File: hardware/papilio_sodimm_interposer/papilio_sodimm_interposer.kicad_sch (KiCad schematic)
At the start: 1 part, among them U1 Papilio Pro

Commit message: Got it going
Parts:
- removed U1: Papilio Pro, papilo_pro:COCOON_48BIT, symbol Papilio_Pro:Papilio_Pro
- added J1: Papilio Pro, Papilio_Pro:PAPILIO_PRO, symbol Papilio_pro:Papilio_Pro
- added SLOT1: DDR3_204P_SMD, Papilio_Pro:SODIMM_DDR3_EDGE, symbol Things:DDR3_204P_SMD
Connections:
- net +5V: now also J1.VIW1@1 (5V), J1.VIW1@2 (5V), J1.VIW1@3 (5V), J1.VIW1@4 (5V), J1.VIW2@1 (5V), J1.VIW2@2 (5V), SLOT1.4, SLOT1.5, SLOT1.6, SLOT1.7
- net GND: now also J1.GNDW1@1 (GND), J1.GNDW1@2 (GND), J1.GNDW1@3 (GND), J1.GNDW1@4 (GND), J1.GNDW2@1 (GND), J1.GNDW2@2 (GND), SLOT1.127, SLOT1.128, SLOT1.13, SLOT1.133, SLOT1.134, SLOT1.138, SLOT1.139, SLOT1.14, SLOT1.144, SLOT1.145, SLOT1.150, SLOT1.151, SLOT1.155, SLOT1.156, SLOT1.161, SLOT1.162, SLOT1.167, SLOT1.168, SLOT1.172, SLOT1.173, SLOT1.178, SLOT1.179, SLOT1.184, SLOT1.185, SLOT1.189, SLOT1.19, SLOT1.190, SLOT1.195, SLOT1.196, SLOT1.2, SLOT1.20, SLOT1.25, SLOT1.26, SLOT1.3, SLOT1.31, SLOT1.32, SLOT1.37, SLOT1.38, SLOT1.43, SLOT1.48, SLOT1.49, SLOT1.54, SLOT1.55, SLOT1.60, SLOT1.61, SLOT1.66, SLOT1.71, SLOT1.72, SLOT1.8, SLOT1.9, SLOT1.MP
- new net: J1.3V3W1@1 (3.3V), J1.3V3W1@2 (3.3V), J1.3V3W1@3 (3.3V), J1.3V3W1@4 (3.3V), J1.3V3W2@1 (3.3V), J1.3V3W2@2 (3.3V)
- new net +3.3V: SLOT1.22, SLOT1.24
- new net A13_IOR32A_READY: SLOT1.98
- new net B10_IOR31B_~{RECFG}: SLOT1.96
- new net C10_IOR39A: SLOT1.135
- new net C13_IOR32B_DONE: SLOT1.136
- new net C7_IOL40B_1V5: SLOT1.157
- new net CLK16: SLOT1.148
- new net CLK_16: J1.A13
- new net D7_IOL53B_1V5: SLOT1.159
- new net E8_IOL45B_1V5: SLOT1.160
- new net E9_IOL38B_1V5: SLOT1.158
- new net FPGA_CS#: J1.B9, SLOT1.198
- new net FPGA_MISO: J1.B10, SLOT1.192
- new net FPGA_MOSI: J1.B11, SLOT1.194
- new net FPGA_SCLK: J1.B12, SLOT1.200
- new net F_VCCO0&1: SLOT1.164, SLOT1.166
- new net F_VCCO7: SLOT1.170, SLOT1.174
- new net JTAG_TCK: SLOT1.149
- new net JTAG_TDI: SLOT1.153
- new net JTAG_TDO: SLOT1.147
- new net JTAG_TMS: SLOT1.143
- new net LVDS_IOR40_N: SLOT1.193
- new net LVDS_IOR40_P: SLOT1.191
- new net LVDS_IOT32_N: SLOT1.152
- new net LVDS_IOT32_P: SLOT1.154
- new net LVDS_TX1_N: SLOT1.142
- new net LVDS_TX1_P: SLOT1.140
- new net M11_IOR27B_FPGA_TXO: SLOT1.11
- new net R09_I1: SLOT1.63
- new net R09_Q1: SLOT1.65
- new net R10_I1: J1.A10, SLOT1.62
- new net R10_Q1: SLOT1.64
- new net R11_I1: J1.A9, SLOT1.67
- new net R11_Q1: SLOT1.69
- new net R12_I1: J1.A11, SLOT1.68
- new net R12_Q1: SLOT1.70
- new net R13_I1: J1.A1, SLOT1.73
- new net R13_Q1: SLOT1.75
- new net R14_I1: J1.A0, SLOT1.74
- new net R14_Q1: SLOT1.76
- new net R15_I1: J1.A2, SLOT1.77
- new net R15_Q1: SLOT1.79
- new net R16_I1: J1.A5, SLOT1.78
- new net R16_Q1: SLOT1.80
- new net R17_I1: J1.A6, SLOT1.83
- new net R17_Q1: SLOT1.85
- new net R18_I1: J1.A4, SLOT1.84
- new net R18_Q1: SLOT1.86
- new net R19_I1: J1.C1, SLOT1.89
- new net R19_Q1: SLOT1.91
- new net R20_I1: J1.C0, SLOT1.90
- new net R20_Q1: SLOT1.92
- new net R21_I1: J1.C2, SLOT1.95
- new net R21_Q1: SLOT1.97
- new net R22_I1: J1.C5, SLOT1.101
- new net R22_Q1: SLOT1.103
- new net R23_I1: J1.C6, SLOT1.107
- new net R23_Q1: SLOT1.109
- new net R24_I1: J1.C4, SLOT1.113
- new net R24_Q1: SLOT1.115
- new net R25_I1: SLOT1.119
- new net R25_Q1: SLOT1.121
- new net R26_I1: SLOT1.123
- new net R26_Q1: SLOT1.125
- new net R27_I1: SLOT1.129
- new net R27_Q1: SLOT1.131
- new net R28_I1: SLOT1.130
- new net R28_Q1: SLOT1.132
- new net R29_I1: SLOT1.175
- new net R29_Q1: SLOT1.177
- new net R30_I1: SLOT1.180
- new net R30_Q1: SLOT1.176
- new net R31_I1: SLOT1.181
- new net R31_Q1: SLOT1.183
- new net R32_I1: SLOT1.186
- new net R32_Q1: SLOT1.182
- new net R9_I1: J1.A12
- new net RADIO_RECONFIG: SLOT1.146
- new net RX01_I0: SLOT1.27
- new net RX01_I1: J1.C13, SLOT1.29
- new net RX01_Q0: SLOT1.28
- new net RX01_Q1: SLOT1.30
- new net RX02_I0: SLOT1.33
- new net RX02_I1: J1.C14, SLOT1.35
- new net RX02_Q0: SLOT1.34
- new net RX02_Q1: SLOT1.36
- new net RX03_I0: SLOT1.39
- new net RX03_I1: J1.C12, SLOT1.41
- new net RX03_Q0: SLOT1.40
- new net RX03_Q1: SLOT1.42
- new net RX04_I0: SLOT1.45
- new net RX04_I1: J1.C10, SLOT1.47
- new net RX04_Q0: SLOT1.44
- new net RX04_Q1: SLOT1.46
- new net RX05_I1: J1.C9, SLOT1.51
- new net RX05_Q1: SLOT1.53
- new net RX06_I1: J1.C11, SLOT1.50
- new net RX06_Q1: SLOT1.52
- new net RX07_I1: J1.A14, SLOT1.57
- new net RX07_Q1: SLOT1.59
- new net RX08_I1: J1.A15, SLOT1.58
- new net RX08_Q1: SLOT1.56
- new net T10_IOR35B_FPGA_~{RST}: SLOT1.15
- new net T13_IOR8B_FPGA_RXO: SLOT1.1
- new net T15_IOR7A: SLOT1.81
- new net T2_IOB48B_1V5: SLOT1.163
- new net T3_IOB52B_1V5: SLOT1.165
- new net T4_IOB45B_1V5: SLOT1.169
- new net T5_IOB54B_1V5: SLOT1.171
- no-connect marks 18 -> 96
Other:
- removed sheet Connectors
- note added: "0/IOR7A/F13"
- note added: "0/IOR7A/G12"
- note added: "0/IOT13A/G15"
- note added: "0/IOT13B/G14"
- note added: "0/IOT14A/G11"
- note added: "0/IOT14B/H12"
- note added: "0/IOT16A/G16"
- note added: "0/IOT16B/H15"
- note added: "0/IOT18A/H13"
- note added: "0/IOT18B/J12"
- note added: "0/IOT20A/H14"
- note added: "0/IOT20B/H16"
- note added: "0/IOT22A/J16"
- note added: "0/IOT22B/J14"
- note added: "0/IOT24A/J15"
- note added: "0/IOT24B/K16"
- note added: "0/IOT4A/D16"
- note added: "0/IOT4B/E14"
- note added: "0/IOT6A/E15"
- note added: "0/IOT6B/F15"
- note added: "0/IOT9A/F14"
- note added: "0/IOT9B/F16"
- note added: "1/IOT32A/J11"
- note added: "1/IOT32B/L12"
- note added: "1/IOT34A/L16"
- note added: "1/IOT34B/L14"
- note added: "1/IOT36A/K13"
- note added: "1/IOT36B/K12"
- note added: "1/IOT38A/K11"
- note added: "1/IOT38B/L13"
- note added: "1/IOT40A/M14"
- note added: "1/IOT40B/M15"
- note added: "1/IOT44A/D14"
- note added: "1/IOT44B/E15"
- note added: "1/IOT48A/N15"
- note added: "1/IOT48B/P16"
- note added: "1/IOT4A/K14"
- note added: "1/IOT4B/K15"
- note added: "1/IOT52A/N16"
- note added: "1/IOT52B/N14"
- note added: "1/IOT54A/P15"
- note added: "1/IOT54B/R16"
- note added: "2/IOR11A/R12"
- note added: "2/IOR11B/P13"
- note added: "2/IOR17A/R11"
- note added: "2/IOR17B/T12"
- note added: "2/IOR20A/R13"
- note added: "2/IOR20B/T14"
- note added: "2/IOR24A/T11"
- note added: "2/IOR24B/P11"
- note added: "2/IOR25A/C6"
- note added: "2/IOR25B/B8"
- note added: "2/IOR26A/A7"
- note added: "2/IOR26B/A6"
- note added: "2/IOR7A/T15"
- note added: "2/IOR8B/T13"
- note added: "204P DDR3 SODIMM CONNECTOR TO CORRELATOR"
- note added: "3/IOR27B/M11"
- note added: "3/IOR29A/T7"
- note added: "3/IOR29B/R8"
- note added: "3/IOR31A/A13"
- note added: "3/IOR31B/B10"
- note added: "3/IOR32B/C13"
- note added: "3/IOR35A/R9"
- note added: "3/IOR35B/T10"
- note added: "3/IOR36B/N9"
- note added: "3/IOR38A/T9"
- note added: "3/IOR38B/P9"
- note added: "3/IOR39A/C10"
- note added: "3/IOR40A/N8"
- note added: "3/IOR40B/L9"
- note added: "3/IOR42A/T8"
- note added: "3/IOR42B/P8"
- note added: "3/IOR44A/M6"
- note added: "3/IOR44B/L8"
- note added: "3/IOR47B/N7"
- note added: "3/IOR49A/R7"
- note added: "3/IOR49B/P7"
- note added: "3/IOR51A/N6"
- note added: "3/IOR53A/P6"
- note added: "3/IOR53B/T6"
- note added: "4/IOB45B/T4"
- note added: "4/IOB48B/T2"
- note added: "4/IOB52B/T3"
- note added: "4/IOB54B/T5"
- note added: "4/IOL38B/E9"
- note added: "4/IOL40B/C7"
- note added: "4/IOL45B/E8"
- note added: "4/IOL53B/D7"
- note added: "7/IOL11A/F10"
- note added: "7/IOL13A/B11"
- note added: "7/IOL13B/A12"
- note added: "7/IOL15A/A11"
- note added: "7/IOL15B/C11"
- note added: "7/IOL17A/D10"
- note added: "7/IOL17B/E10"
- note added: "7/IOL22A/D11"
- note added: "7/IOL27A/A9"
- note added: "7/IOL27B/C9"
- note added: "7/IOL2A/B14"
- note added: "7/IOL2B/A15"
- note added: "7/IOL7A/C12"
- note added: "7/IOL7B/B12"
- note added: "7/IOL8A/B13"
- note added: "7/IOL8B/A14"
- note added: "Part A: 32 GPIO available Part B: RHS. 20 GPIO Part B: LHS. 30 GPIO Total. 81 Avalable (as GCLK for radio uses one)"
- note added: "Vcc Bank0/1 = 3.3V"
- note added: "Vcc Bank2 = 3.3V"
- note added: "Vcc Bank3 = 3.3V"
- note added: "Vcc Bank4/5/6 = 1.5V"
- note added: "Vcc Bank7 = 3.3V"
- note removed: "This work is licenced under the GPL v3 or later."

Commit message: Update interposer and clock test
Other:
- company: University of Otago, Gadget Factory LLC -> Tim Molteno. Electronic Research Foundation
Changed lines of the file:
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@@
 	(title_block
 		(title "Papilio Pro Interposer")
-		(date "2024-02-29")
+		(date "2024-04-15")
 		(rev "1.0")
-		(company "University of Otago, Gadget Factory LLC")
-		(comment 1 "©Phill Brown 2024, Gadget Factory 2009-2012")
+		(company "Tim Molteno. Electronic Research Foundation")
+		(comment 1 "©Tim Molteno 2024, ")
 	)
 	(bus_alias ""

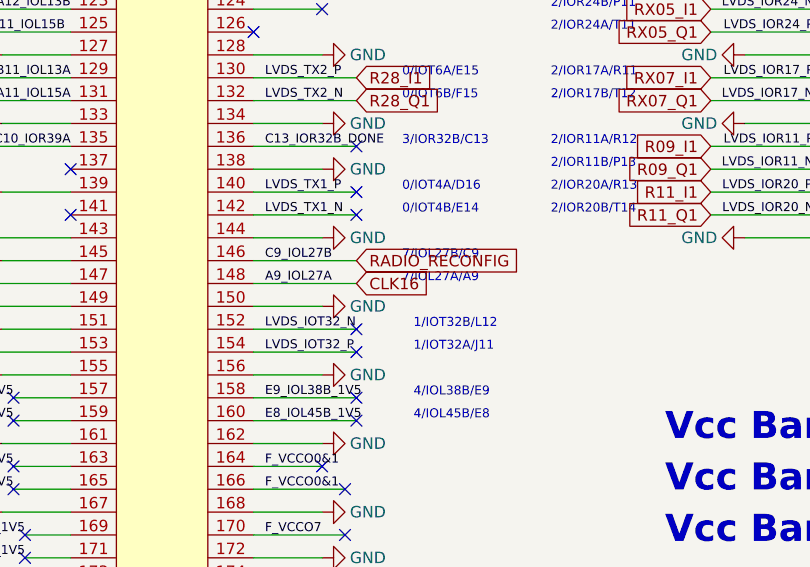
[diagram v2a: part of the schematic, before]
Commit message: Update the footprints and layout
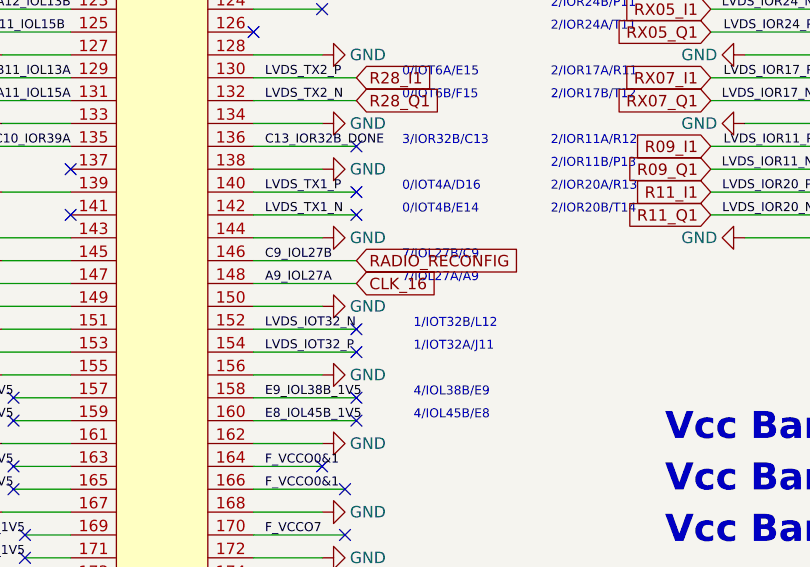
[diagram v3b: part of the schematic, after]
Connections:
- net CLK16 is gone; now on net CLK_16: SLOT1.148
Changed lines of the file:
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@@
 		)
 	)
-	(global_label "CLK16"
+	(global_label "CLK_16"
 		(shape input)
 		(at 87.63 118.11 0)
@@
 		)
 		(property "Intersheetrefs" "${INTERSHEET_REFS}"
-			(at 96.6023 118.11 0)
+			(at 97.5699 118.11 0)
 			(effects
 				(font
